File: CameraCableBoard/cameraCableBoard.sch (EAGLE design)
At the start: 1 part, among them J2 FLEXCABLE-SFW15R-1STE1LF

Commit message: Worked on camera board
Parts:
- added U$1: DB15, SparkFun-Retired:DB15
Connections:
- new net 3.3V: J2.15
- new net CON_CLKN: J2.8
- new net CON_CLKP: J2.9
- new net CON_D0N: J2.2, U$1.6
- new net CON_D0P: J2.3, U$1.11
- new net CON_D1N: J2.5
- new net CON_D1P: J2.6
- new net ENABLE: J2.11
- new net GND: J2.1, J2.10, J2.4, J2.7, U$1.1, U$1.7
- new net N$10: U$1.13
- new net N$11: U$1.8
- new net N$12: U$1.9
- new net N$13: U$1.14
- new net N$14: U$1.10
- new net N$15: U$1.15
- new net N$2: U$1.2
- new net N$3: U$1.3
- new net N$4: U$1.4
- new net N$5: U$1.5
- new net N$9: U$1.12
- new net SCL: J2.13
- new net SDA: J2.14
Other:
- note added: "Connect to Bundle to Cam"
- note added: "Connect to Ribbon to RPi"
- note added: "This side imitates the RPi side"
- note added: "This side imitates the camera side of the connection"
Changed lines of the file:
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@@
 <part name="FRAME1" library="frames" library_urn="urn:adsk.eagle:library:229" deviceset="A4L-LOC" device=""/>
 <part name="J2" library="RPi-Parts" deviceset="FLEXCABLE-SFW15R-1STE1LF" device=""/>
+<part name="U$1" library="SparkFun-Retired" library_urn="urn:adsk.eagle:library:533" deviceset="DB15" device=""/>
 </parts>
 <sheets>
@@
 </text>
 <text x="15.24" y="167.64" size="1.778" layer="97">https://www.digikey.com/product-detail/en/amphenol-icc-fci/SFW15R-2STE1LF/609-1906-1-ND/1003189</text>
+<text x="15.24" y="142.24" size="2.54" layer="97">This side imitates the camera side of the connection</text>
+<text x="15.24" y="147.32" size="2.54" layer="97">Connect to Ribbon to RPi</text>
+<text x="111.76" y="144.78" size="2.54" layer="97">Connect to Bundle to Cam</text>
+<text x="111.76" y="139.7" size="2.54" layer="97">This side imitates the RPi side</text>
 </plain>
 <instances>
@@
 <attribute name="VALUE" x="15.234459375" y="88.8723" size="1.779940625" layer="96"/>
 </instance>
+<instance part="U$1" gate="G$1" x="119.38" y="116.84" smashed="yes">
+<attribute name="VALUE" x="115.57" y="98.425" size="1.778" layer="96" font="vector"/>
+<attribute name="NAME" x="115.57" y="130.81" size="1.778" layer="95" font="vector"/>
+</instance>
 </instances>
 <busses>
 </busses>
 <nets>
+<net name="GND" class="0">
+<segment>
+<pinref part="J2" gate="G$1" pin="1"/>
+<wire x1="30.48" y1="134.62" x2="33.02" y2="134.62" width="0.1524" layer="91"/>
+<label x="33.02" y="134.62" size="1.27" layer="95" xref="yes"/>
+</segment>
+<segment>
+<pinref part="J2" gate="G$1" pin="4"/>
+<wire x1="30.48" y1="127" x2="33.02" y2="127" width="0.1524" layer="91"/>
+<label x="33.02" y="127" size="1.27" layer="95" xref="yes"/>
+</segment>
+<segment>
+<pinref part="J2" gate="G$1" pin="7"/>
+<wire x1="30.48" y1="119.38" x2="33.02" y2="119.38" width="0.1524" layer="91"/>
+<label x="33.02" y="119.38" size="1.27" layer="95" xref="yes"/>
+</segment>
+<segment>
+<pinref part="J2" gate="G$1" pin="10"/>
+<wire x1="30.48" y1="111.76" x2="33.02" y2="111.76" width="0.1524" layer="91"/>
+<label x="33.02" y="111.76" size="1.27" layer="95" xref="yes"/>
+</segment>
+<segment>
+<pinref part="U$1" gate="G$1" pin="1"/>
+<wire x1="111.76" y1="124.46" x2="109.22" y2="124.46" width="0.1524" layer="91"/>
+<label x="109.22" y="124.46" size="1.27" layer="95" rot="R180" xref="yes"/>
+</segment>
+<segment>
+<pinref part="U$1" gate="G$1" pin="7"/>
+<wire x1="127.254" y1="121.92" x2="129.54" y2="121.92" width="0.1524" layer="91"/>
+<label x="129.54" y="121.92" size="1.27" layer="95" xref="yes"/>
+</segment>
+</net>
+<net name="CON_D0N" class="0">
+<segment>
+<pinref part="J2" gate="G$1" pin="2"/>
+<wire x1="30.48" y1="132.08" x2="33.02" y2="132.08" width="0.1524" layer="91"/>
+<label x="33.02" y="132.08" size="1.27" layer="95" xref="yes"/>
+</segment>
+<segment>
+<pinref part="U$1" gate="G$1" pin="6"/>
+<wire x1="127.254" y1="127" x2="129.54" y2="127" width="0.1524" layer="91"/>
+<label x="129.54" y="127" size="1.27" layer="95" xref="yes"/>
+</segment>
+</net>
+<net name="CON_D0P" class="0">
+<segment>
+<pinref part="J2" gate="G$1" pin="3"/>
+<wire x1="30.48" y1="129.54" x2="33.02" y2="129.54" width="0.1524" layer="91"/>
+<label x="33.02" y="129.54" size="1.27" layer="95" xref="yes"/>
+</segment>
+<segment>
+<pinref part="U$1" gate="G$1" pin="11"/>
+<wire x1="127.254" y1="124.46" x2="129.54" y2="124.46" width="0.1524" layer="91"/>
+<label x="129.54" y="124.46" size="1.27" layer="95" xref="yes"/>
+</segment>
+</net>
+<net name="CON_D1N" class="0">
+<segment>
+<pinref part="J2" gate="G$1" pin="5"/>
+<wire x1="30.48" y1="124.46" x2="33.02" y2="124.46" width="0.1524" layer="91"/>
+<label x="33.02" y="124.46" size="1.27" layer="95" xref="yes"/>
+</segment>
+</net>
+<net name="CON_D1P" class="0">
+<segment>
+<pinref part="J2" gate="G$1" pin="6"/>
+<wire x1="30.48" y1="121.92" x2="33.02" y2="121.92" width="0.1524" layer="91"/>
+<label x="33.02" y="121.92" size="1.27" layer="95" xref="yes"/>
+</segment>
+</net>
+<net name="CON_CLKN" class="0">
+<segment>
+<pinref part="J2" gate="G$1" pin="8"/>
+<wire x1="30.48" y1="116.84" x2="33.02" y2="116.84" width="0.1524" layer="91"/>
+<label x="33.02" y="116.84" size="1.27" layer="95" xref="yes"/>
+</segment>
+</net>
+<net name="CON_CLKP" class="0">
+<segment>
+<pinref part="J2" gate="G$1" pin="9"/>
+<wire x1="30.48" y1="114.3" x2="33.02" y2="114.3" width="0.1524" layer="91"/>
+<label x="33.02" y="114.3" size="1.27" layer="95" xref="yes"/>
+</segment>
+</net>
+<net name="ENABLE" class="0">
+<segment>
+<pinref part="J2" gate="G$1" pin="11"/>
+<wire x1="30.48" y1="109.22" x2="33.02" y2="109.22" width="0.1524" layer="91"/>
+<label x="33.02" y="109.22" size="1.27" layer="95" xref="yes"/>
+</segment>
+</net>
+<net name="SCL" class="0">
+<segment>
+<pinref part="J2" gate="G$1" pin="13"/>
+<wire x1="30.48" y1="104.14" x2="33.02" y2="104.14" width="0.1524" layer="91"/>
+<label x="33.02" y="104.14" size="1.27" layer="95" xref="yes"/>
+</segment>
+</net>
+<net name="SDA" class="0">
+<segment>
+<pinref part="J2" gate="G$1" pin="14"/>
+<wire x1="30.48" y1="101.6" x2="33.02" y2="101.6" width="0.1524" layer="91"/>
+<label x="33.02" y="101.6" size="1.27" layer="95" xref="yes"/>
+</segment>
+</net>
+<net name="3.3V" class="0">
+<segment>
+<pinref part="J2" gate="G$1" pin="15"/>
+<wire x1="30.48" y1="99.06" x2="33.02" y2="99.06" width="0.1524" layer="91"/>
+<label x="33.02" y="99.06" size="1.27" layer="95" xref="yes"/>
+</segment>
+</net>
+<net name="N$2" class="0">
+<segment>
+<pinref part="U$1" gate="G$1" pin="2"/>
+<wire x1="111.76" y1="119.38" x2="109.22" y2="119.38" width="0.1524" layer="91"/>
+<label x="109.22" y="119.38" size="1.27" layer="95" rot="R180" xref="yes"/>
+</segment>
+</net>
+<net name="N$3" class="0">
+<segment>
+<pinref part="U$1" gate="G$1" pin="3"/>
+<wire x1="111.76" y1="114.3" x2="109.22" y2="114.3" width="0.1524" layer="91"/>
+<label x="109.22" y="114.3" size="1.27" layer="95" rot="R180" xref="yes"/>
+</segment>
+</net>
+<net name="N$4" class="0">
+<segment>
+<pinref part="U$1" gate="G$1" pin="4"/>
+<wire x1="111.76" y1="109.22" x2="109.22" y2="109.22" width="0.1524" layer="91"/>
+<label x="109.22" y="109.22" size="1.27" layer="95" rot="R180" xref="yes"/>
+</segment>
+</net>
+<net name="N$5" class="0">
+<segment>
+<pinref part="U$1" gate="G$1" pin="5"/>
+<wire x1="111.76" y1="104.14" x2="109.22" y2="104.14" width="0.1524" layer="91"/>
+<label x="109.22" y="104.14" size="1.27" layer="95" rot="R180" xref="yes"/>
+</segment>
+</net>
+<net name="N$9" class="0">
+<segment>
+<pinref part="U$1" gate="G$1" pin="12"/>
+<wire x1="127.254" y1="119.38" x2="129.54" y2="119.38" width="0.1524" layer="91"/>
+<label x="129.54" y="119.38" size="1.27" layer="95" xref="yes"/>
+</segment>
+</net>
+<net name="N$10" class="0">
+<segment>
+<pinref part="U$1" gate="G$1" pin="13"/>
+<wire x1="127.254" y1="114.3" x2="129.54" y2="114.3" width="0.1524" layer="91"/>
+<label x="129.54" y="114.3" size="1.27" layer="95" xref="yes"/>
+</segment>
+</net>
+<net name="N$11" class="0">
+<segment>
+<pinref part="U$1" gate="G$1" pin="8"/>
+<wire x1="127.254" y1="116.84" x2="129.54" y2="116.84" width="0.1524" layer="91"/>
+<label x="129.54" y="116.84" size="1.27" layer="95" xref="yes"/>
+</segment>
+</net>
+<net name="N$12" class="0">
+<segment>
+<pinref part="U$1" gate="G$1" pin="9"/>
+<wire x1="127.254" y1="111.76" x2="129.54" y2="111.76" width="0.1524" layer="91"/>
+<label x="129.54" y="111.76" size="1.27" layer="95" xref="yes"/>
+</segment>
+</net>
+<net name="N$13" class="0">
+<segment>
+<pinref part="U$1" gate="G$1" pin="14"/>
+<wire x1="127.254" y1="109.22" x2="129.54" y2="109.22" width="0.1524" layer="91"/>
+<label x="129.54" y="109.22" size="1.27" layer="95" xref="yes"/>
+</segment>
+</net>
+<net name="N$14" class="0">
+<segment>
+<pinref part="U$1" gate="G$1" pin="10"/>
+<wire x1="127.254" y1="106.68" x2="129.54" y2="106.68" width="0.1524" layer="91"/>
+<label x="129.54" y="106.68" size="1.27" layer="95" xref="yes"/>
+</segment>
+</net>
+<net name="N$15" class="0">
+<segment>
+<pinref part="U$1" gate="G$1" pin="15"/>
+<wire x1="127.254" y1="104.14" x2="129.54" y2="104.14" width="0.1524" layer="91"/>
+<label x="129.54" y="104.14" size="1.27" layer="95" xref="yes"/>
+</segment>
+</net>
 </nets>
 </sheet>

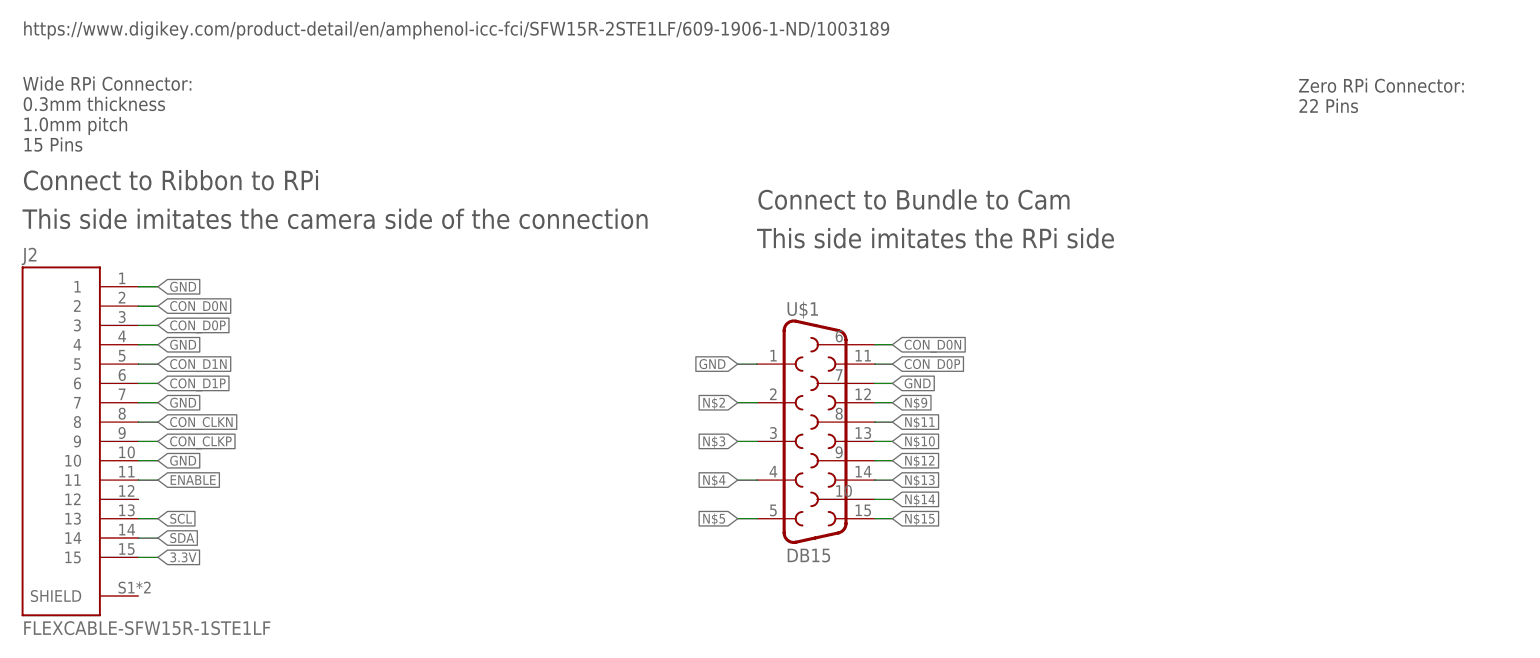
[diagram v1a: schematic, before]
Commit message: Added board-edge db15, ready to route camera signal converter board
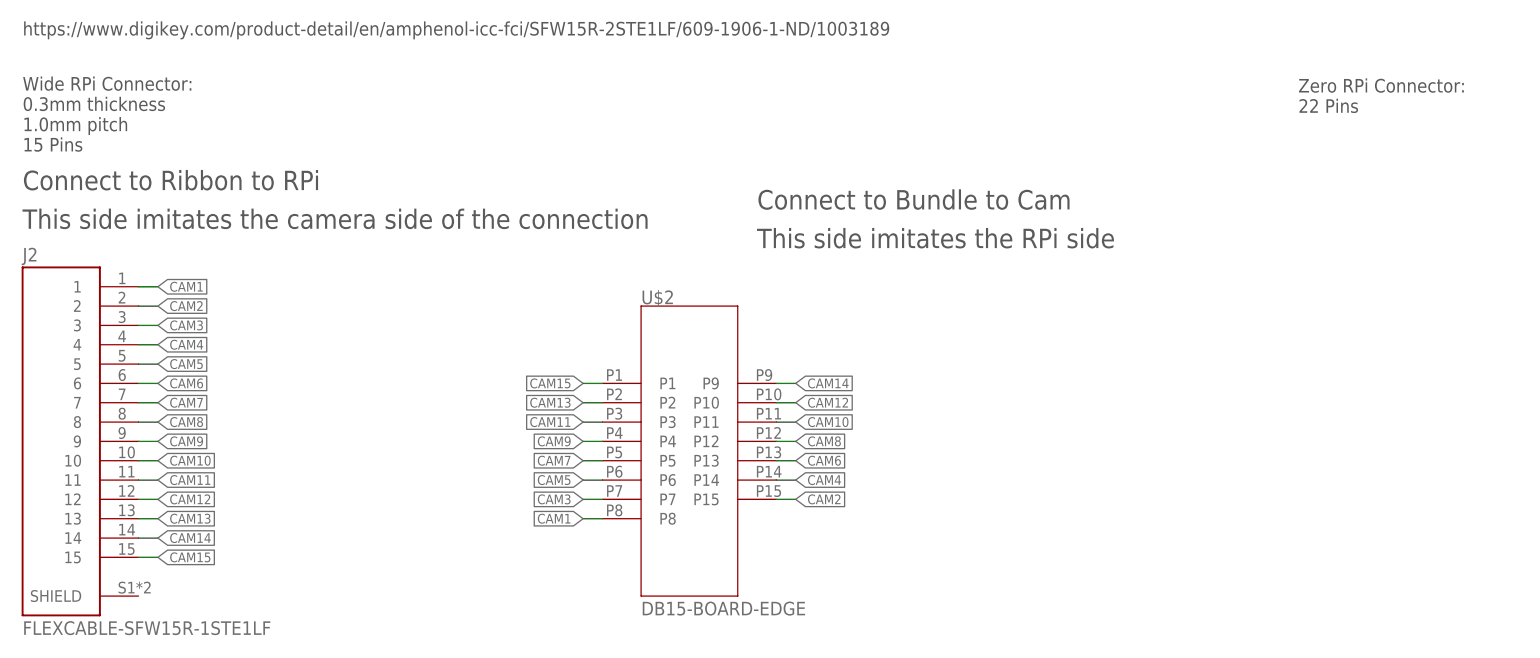
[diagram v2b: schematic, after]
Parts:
- removed U$1: DB15, SparkFun-Retired:DB15
- added U$2: DB15-BOARD-EDGE, RPi-Parts:DB15-BOARD-EDGE
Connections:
- removed net 3.3V: J2.15
- removed net CON_CLKN: J2.8
- removed net CON_CLKP: J2.9
- removed net CON_D0N: J2.2, U$1.6
- removed net CON_D0P: J2.3, U$1.11
- removed net CON_D1N: J2.5
- removed net CON_D1P: J2.6
- removed net ENABLE: J2.11
- removed net GND: J2.1, J2.10, J2.4, J2.7, U$1.1, U$1.7
- removed net N$10: U$1.13
- removed net N$11: U$1.8
- removed net N$12: U$1.9
- removed net N$13: U$1.14
- removed net N$14: U$1.10
- removed net N$15: U$1.15
- removed net N$2: U$1.2
- removed net N$3: U$1.3
- removed net N$4: U$1.4
- removed net N$5: U$1.5
- removed net N$9: U$1.12
- removed net SCL: J2.13
- removed net SDA: J2.14
- new net CAM1: J2.1, U$2.P8
- new net CAM10: J2.10, U$2.P11
- new net CAM11: J2.11, U$2.P3
- new net CAM12: J2.12, U$2.P10
- new net CAM13: J2.13, U$2.P2
- new net CAM14: J2.14, U$2.P9
- new net CAM15: J2.15, U$2.P1
- new net CAM2: J2.2, U$2.P15
- new net CAM3: J2.3, U$2.P7
- new net CAM4: J2.4, U$2.P14
- new net CAM5: J2.5, U$2.P6
- new net CAM6: J2.6, U$2.P13
- new net CAM7: J2.7, U$2.P5
- new net CAM8: J2.8, U$2.P12
- new net CAM9: J2.9, U$2.P4
